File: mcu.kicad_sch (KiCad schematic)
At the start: 23 parts, among them IC3 STM32G473RCT6, J1 USB4105-GF-A-120, Y1 ECS-240-6-37B-7KM-TR

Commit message: reorganized everything and switched to 0603 as a minimum size
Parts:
- C10, C11, C24, C25, C3, C4, C5, C6, C7, C8, C9: footprint Capacitor_SMD:C_0402_1005Metric -> Capacitor_SMD:C_0603_1608Metric
- R10, R11, R15, R22, R23, R9: footprint Resistor_SMD:R_0402_1005Metric -> Resistor_SMD:R_0603_1608Metric
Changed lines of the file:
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@@
 			)
 		)
-		(property "Footprint" "Resistor_SMD:R_0402_1005Metric"
+		(property "Footprint" "Resistor_SMD:R_0603_1608Metric"
 			(at 82.55 72.898 90)
 			(effects
@@
 			)
 		)
-		(property "Datasheet" "https://www.lcsc.com/datasheet/C60490.pdf"
+		(property "Datasheet" "~"
 			(at 82.55 71.12 0)
 			(effects
@@
 			)
 		)
-		(property "Footprint" "Capacitor_SMD:C_0402_1005Metric"
+		(property "Footprint" "Capacitor_SMD:C_0603_1608Metric"
 			(at 25.4 81.5848 0)
 			(effects
@@
 			)
 		)
-		(property "Datasheet" "https://www.lcsc.com/datasheet/C76984.pdf"
+		(property "Datasheet" "~"
 			(at 21.59 82.55 0)
 			(effects
@@
 		)
 		(instances
-			(project ""
+			(project "fcg4"
 				(path "/ebe93c2f-0aae-4f69-99fc-930f63b0ac94/dd494bae-08c6-4b46-92c8-f2c39e9b21e0"
 					(reference "IC3")
@@
 			)
 		)
-		(property "Footprint" "Capacitor_SMD:C_0402_1005Metric"
+		(property "Footprint" "Capacitor_SMD:C_0603_1608Metric"
 			(at 27.6352 111.76 0)
 			(effects
@@
 			)
 		)
-		(property "Datasheet" "https://www.lcsc.com/datasheet/C76984.pdf"
+		(property "Datasheet" "~"
 			(at 26.67 107.95 0)
 			(effects
@@
 			)
 		)
-		(property "Footprint" "Capacitor_SMD:C_0402_1005Metric"
+		(property "Footprint" "Capacitor_SMD:C_0603_1608Metric"
 			(at 106.9848 182.88 0)
 			(effects
@@
 			)
 		)
-		(property "Datasheet" "https://www.lcsc.com/datasheet/C1518208.pdf"
+		(property "Datasheet" "~"
 			(at 107.95 186.69 0)
 			(effects
@@
 			)
 		)
-		(property "Footprint" "Capacitor_SMD:C_0402_1005Metric"
+		(property "Footprint" "Capacitor_SMD:C_0603_1608Metric"
 			(at 243.5352 34.29 0)
 			(effects
@@
 			)
 		)
-		(property "Datasheet" "https://www.lcsc.com/datasheet/C77020.pdf"
+		(property "Datasheet" "~"
 			(at 242.57 30.48 0)
 			(effects
@@
 		)
 		(instances
-			(project ""
+			(project "fcg4"
 				(path "/ebe93c2f-0aae-4f69-99fc-930f63b0ac94/dd494bae-08c6-4b46-92c8-f2c39e9b21e0"
 					(reference "FL1")
@@
 			)
 		)
-		(property "Footprint" "Resistor_SMD:R_0402_1005Metric"
+		(property "Footprint" "Resistor_SMD:R_0603_1608Metric"
 			(at 68.58 66.548 90)
 			(effects
@@
 			)
 		)
-		(property "Datasheet" "https://www.lcsc.com/datasheet/C60490.pdf"
+		(property "Datasheet" "~"
 			(at 68.58 64.77 0)
 			(effects
@@
 			)
 		)
-		(property "Footprint" "Capacitor_SMD:C_0402_1005Metric"
+		(property "Footprint" "Capacitor_SMD:C_0603_1608Metric"
 			(at 262.5852 34.29 0)
 			(effects
@@
 			)
 		)
-		(property "Datasheet" "https://www.lcsc.com/datasheet/C77020.pdf"
+		(property "Datasheet" "~"
 			(at 261.62 30.48 0)
 			(effects
@@
 			)
 		)
-		(property "Footprint" "Capacitor_SMD:C_0402_1005Metric"
+		(property "Footprint" "Capacitor_SMD:C_0603_1608Metric"
 			(at 256.2352 34.29 0)
 			(effects
@@
 			)
 		)
-		(property "Datasheet" "https://www.lcsc.com/datasheet/C77020.pdf"
+		(property "Datasheet" "~"
 			(at 255.27 30.48 0)
 			(effects
@@
 		)
 		(instances
-			(project ""
+			(project "fcg4"
 				(path "/ebe93c2f-0aae-4f69-99fc-930f63b0ac94/dd494bae-08c6-4b46-92c8-f2c39e9b21e0"
 					(reference "Y1")
@@
 			)
 		)
-		(property "Footprint" "Capacitor_SMD:C_0402_1005Metric"
+		(property "Footprint" "Capacitor_SMD:C_0603_1608Metric"
 			(at 98.0948 182.88 0)
 			(effects
@@
 			)
 		)
-		(property "Datasheet" "https://www.lcsc.com/datasheet/C77020.pdf"
+		(property "Datasheet" "~"
 			(at 99.06 186.69 0)
 			(effects
@@
 		)
 		(instances
-			(project ""
+			(project "fcg4"
 				(path "/ebe93c2f-0aae-4f69-99fc-930f63b0ac94/dd494bae-08c6-4b46-92c8-f2c39e9b21e0"
 					(reference "C3")
@@
 			)
 		)
-		(property "Footprint" "Capacitor_SMD:C_0402_1005Metric"
+		(property "Footprint" "Capacitor_SMD:C_0603_1608Metric"
 			(at 249.8852 34.29 0)
 			(effects
@@
 			)
 		)
-		(property "Datasheet" "https://www.lcsc.com/datasheet/C77020.pdf"
+		(property "Datasheet" "~"
 			(at 248.92 30.48 0)
 			(effects
@@
 		)
 		(instances
-			(project ""
+			(project "fcg4"
 				(path "/ebe93c2f-0aae-4f69-99fc-930f63b0ac94/dd494bae-08c6-4b46-92c8-f2c39e9b21e0"
 					(reference "JP1")
@@
 			)
 		)
-		(property "Footprint" "Capacitor_SMD:C_0402_1005Metric"
+		(property "Footprint" "Capacitor_SMD:C_0603_1608Metric"
 			(at 114.6048 179.07 0)
 			(effects
@@
 			)
 		)
-		(property "Datasheet" "https://www.lcsc.com/datasheet/C77020.pdf"
+		(property "Datasheet" "~"
 			(at 115.57 182.88 0)
 			(effects
@@
 			)
 		)
-		(property "Footprint" "Capacitor_SMD:C_0402_1005Metric"
+		(property "Footprint" "Capacitor_SMD:C_0603_1608Metric"
 			(at 124.7648 179.07 0)
 			(effects
@@
 			)
 		)
-		(property "Datasheet" "https://www.lcsc.com/datasheet/C1518208.pdf"
+		(property "Datasheet" "~"
 			(at 125.73 182.88 0)
 			(effects
@@
 			)
 		)
-		(property "Footprint" "Resistor_SMD:R_0402_1005Metric"
+		(property "Footprint" "Resistor_SMD:R_0603_1608Metric"
 			(at 106.68 65.278 90)
 			(effects
@@
 			)
 		)
-		(property "Datasheet" "https://www.lcsc.com/datasheet/C60490.pdf"
+		(property "Datasheet" "~"
 			(at 106.68 63.5 0)
 			(effects
@@
 		)
 		(instances
-			(project ""
+			(project "fcg4"
 				(path "/ebe93c2f-0aae-4f69-99fc-930f63b0ac94/dd494bae-08c6-4b46-92c8-f2c39e9b21e0"
 					(reference "J1")
@@
 			)
 		)
-		(property "Footprint" "Resistor_SMD:R_0402_1005Metric"
+		(property "Footprint" "Resistor_SMD:R_0603_1608Metric"
 			(at 194.31 102.108 90)
 			(effects
@@
 			)
 		)
-		(property "Datasheet" "https://www.lcsc.com/datasheet/C105872.pdf"
+		(property "Datasheet" "~"
 			(at 194.31 100.33 0)
 			(effects
@@
 		)
 		(instances
-			(project ""
+			(project "fcg4"
 				(path "/ebe93c2f-0aae-4f69-99fc-930f63b0ac94/dd494bae-08c6-4b46-92c8-f2c39e9b21e0"
 					(reference "R10")
@@
 			)
 		)
-		(property "Footprint" "Capacitor_SMD:C_0402_1005Metric"
+		(property "Footprint" "Capacitor_SMD:C_0603_1608Metric"
 			(at 35.56 127.3048 0)
 			(effects
@@
 			)
 		)
-		(property "Datasheet" "https://www.lcsc.com/datasheet/C77020.pdf"
+		(property "Datasheet" "~"
 			(at 31.75 128.27 0)
 			(effects
@@
 			)
 		)
-		(property "Footprint" "Resistor_SMD:R_0402_1005Metric"
+		(property "Footprint" "Resistor_SMD:R_0603_1608Metric"
 			(at 194.31 104.648 90)
 			(effects
@@
 			)
 		)
-		(property "Datasheet" "https://www.lcsc.com/datasheet/C105872.pdf"
+		(property "Datasheet" "~"
 			(at 194.31 102.87 0)
 			(effects
@@
 			)
 		)
-		(property "Footprint" "Resistor_SMD:R_0402_1005Metric"
+		(property "Footprint" "Resistor_SMD:R_0603_1608Metric"
 			(at 36.83 104.648 90)
 			(effects
@@
 			)
 		)
-		(property "Datasheet" "https://www.lcsc.com/datasheet/C185439.pdf"
+		(property "Datasheet" "~"
 			(at 36.83 102.87 0)
 			(effects
@@
 		)
 		(instances
-			(project ""
+			(project "fcg4"
 				(path "/ebe93c2f-0aae-4f69-99fc-930f63b0ac94/dd494bae-08c6-4b46-92c8-f2c39e9b21e0"
 					(reference "R9")

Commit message: update routing
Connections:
- no-connect marks 2 -> 14
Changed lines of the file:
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@@
+	)
+	(no_connect
+		(at 113.03 130.81)
+	)
+	(no_connect
+		(at 59.69 130.81)
 	)
 	(no_connect
@@
 	)
 	(no_connect
+		(at 85.09 168.91)
+	)
+	(no_connect
+		(at 113.03 135.89)
+	)
+	(no_connect
+		(at 59.69 133.35)
+	)
+	(no_connect
+		(at 90.17 90.17)
+	)
+	(no_connect
+		(at 82.55 168.91)
+	)
+	(no_connect
+		(at 92.71 168.91)
+	)
+	(no_connect
+		(at 113.03 133.35)
+	)
+	(no_connect
+		(at 59.69 138.43)
+	)
+	(no_connect
 		(at 234.95 106.68)
 	)
+	(no_connect
+		(at 92.71 90.17)
+	)
+	(no_connect
+		(at 59.69 135.89)
+	)
 	(wire

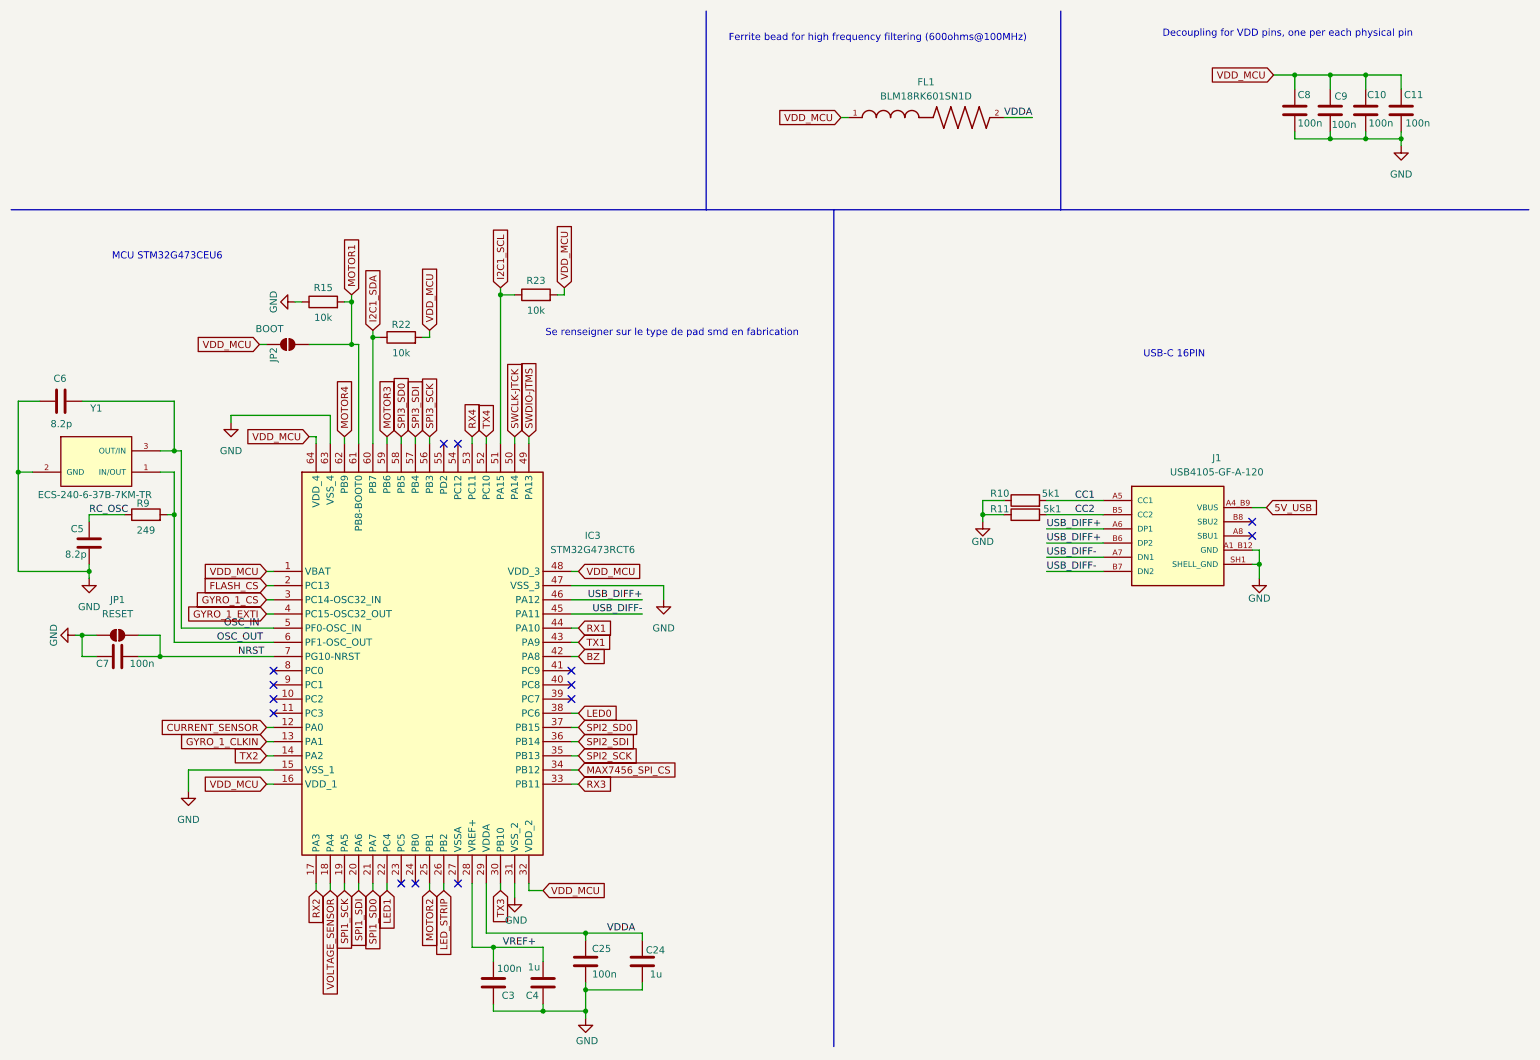
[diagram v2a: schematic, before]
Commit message: changed barometer to BMP580 and completed BOM
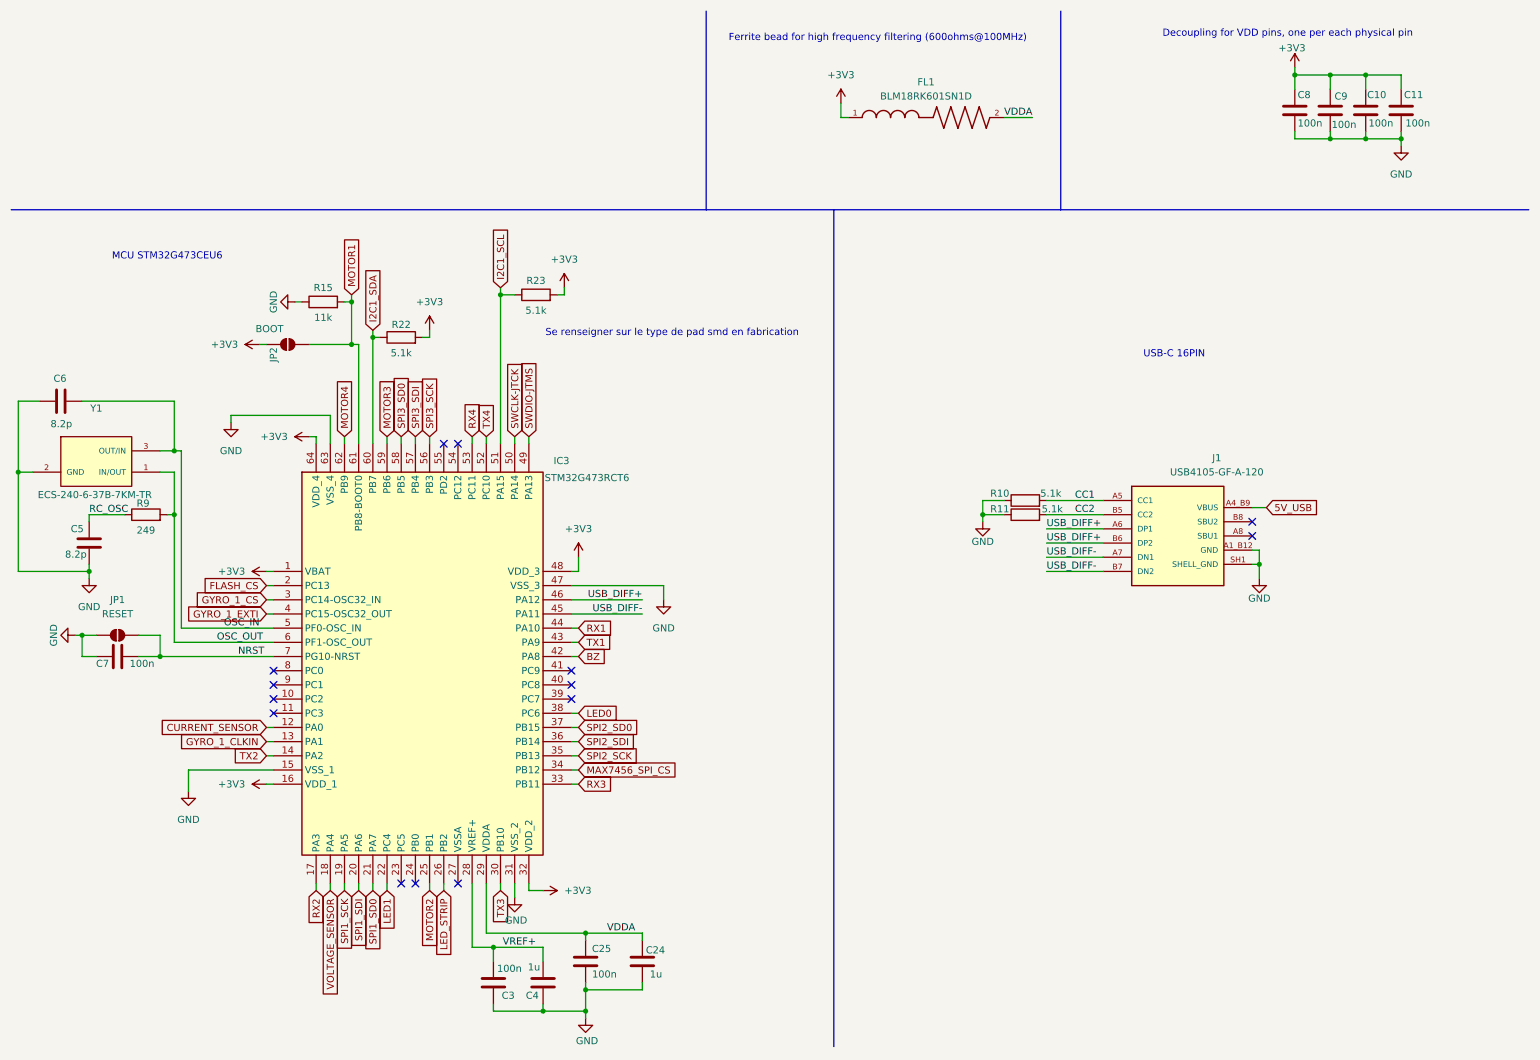
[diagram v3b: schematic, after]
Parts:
- C10, C11, C25, C3, C7, C8, C9: LCSC Part Name C77020 -> C1591; Manufacturer_Name muRata -> Samsung Electro-Mechanics; Manufacturer_Part_Number GRM155R71H104KE14D -> CL10B104KB8NNNC
- C24, C4: LCSC Part Name C1518208 -> C5199872; Manufacturer_Name muRata -> Samsung Electro-Mechanics; Manufacturer_Part_Number GRM155R61H105KE05D -> CL10B105KB8NQNC
- C5, C6: LCSC Part Name C76984 -> C277519; Manufacturer_Name muRata -> YAGEO; Manufacturer_Part_Number GRM1555C1H8R2CA01D -> CC0603CRNPO9BN8R2
- IC3: LCSC Part Name (none) -> C529361
- R10, R11: value 5k1 -> 5.1k; LCSC Part Name C105872 -> C2907044; Manufacturer_Name YAGEO -> FOJAN; Manufacturer_Part_Number RC0402FR-075K1L -> FRC0603F5101TS
- R15: value 10k -> 11k; LCSC Part Name C60490 -> C25950; Manufacturer_Name YAGEO -> UNI-ROYAL; Manufacturer_Part_Number RC0402FR-0710KL -> 0603WAF1102T5E
- R22, R23: value 10k -> 5.1k; LCSC Part Name C60490 -> C2907044; Manufacturer_Name YAGEO -> FOJAN; Manufacturer_Part_Number RC0402FR-0710KL -> FRC0603F5101TS
- R9: LCSC Part Name C185439 -> C2933176; Manufacturer_Name YAGEO -> FOJAN; Manufacturer_Part_Number RC0402FR-07249RL -> FRC0603F2490TS
- Y1: LCSC Part Name (none) -> C5213675
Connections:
- net VDD_MCU renamed +3V3

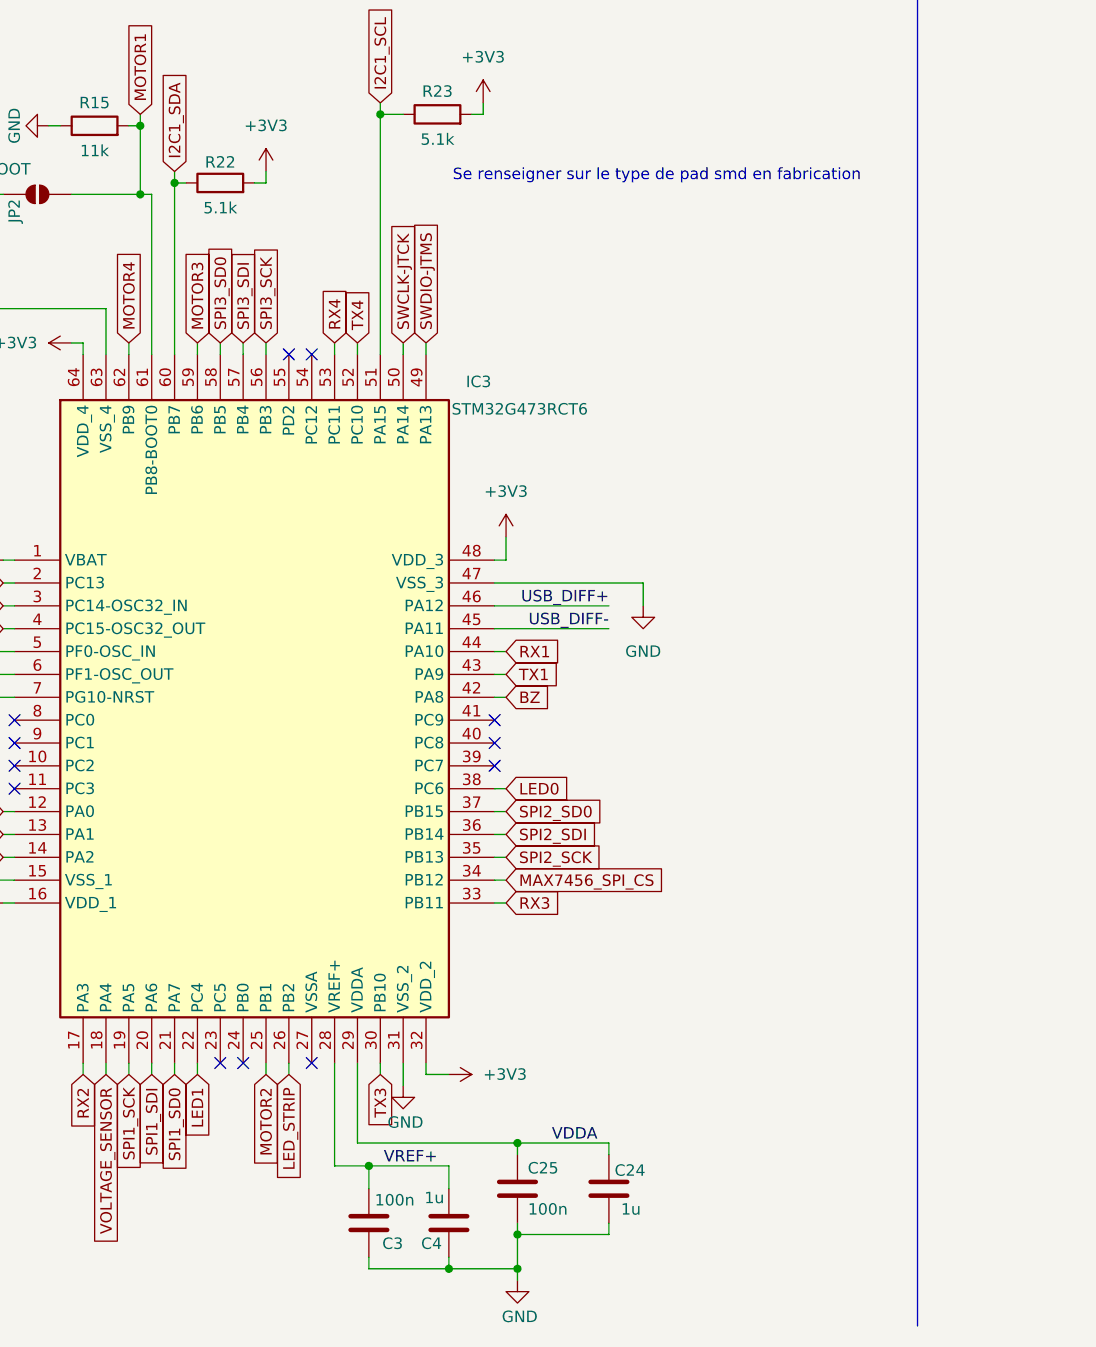
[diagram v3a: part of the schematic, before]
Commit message: switch IMU to BMI270
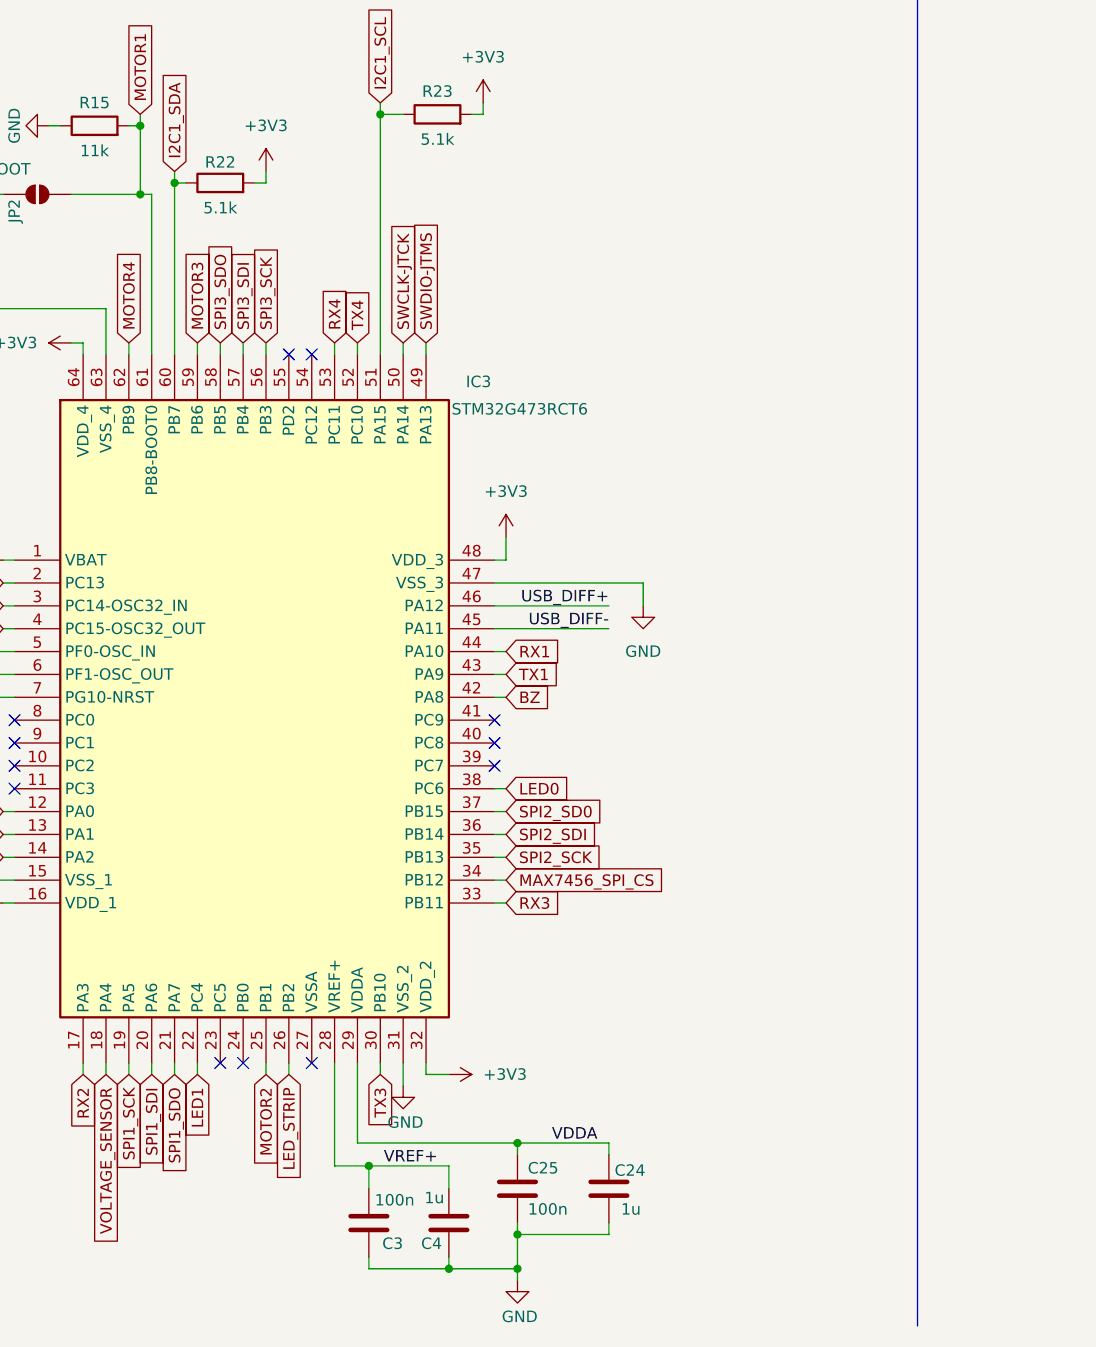
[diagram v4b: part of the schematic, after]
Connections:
- net SPI1_SD0 renamed SPI1_SDO
- net SPI3_SD0 renamed SPI3_SDO
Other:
- note removed: "Se renseigner sur le type de pad smd en fabrication"
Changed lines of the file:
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@@
 	(generator_version "9.0")
 	(paper "A4")
-	(text "Se renseigner sur le type de pad smd en fabrication"
-		(exclude_from_sim no)
-		(at 131.064 70.358 0)
-		(effects
-			(font
-				(size 1.27 1.27)
-			)
-		)
-	)
 	(text "USB-C 16PIN "
 		(exclude_from_sim no)
@@
 		)
 	)
-	(global_label "SPI3_SD0"
+	(global_label "SPI3_SDO"
 		(shape input)
 		(at 82.55 88.9 90)
@@
 		)
 		(property "Intersheetrefs" "${INTERSHEET_REFS}"
-			(at 82.55 76.9644 90)
+			(at 82.55 76.8434 90)
 			(effects
 				(font
@@
 		)
 	)
-	(global_label "SPI1_SD0"
+	(global_label "SPI1_SDO"
 		(shape input)
 		(at 77.47 170.18 270)
@@
 		)
 		(property "Intersheetrefs" "${INTERSHEET_REFS}"
-			(at 77.47 182.1156 90)
+			(at 77.47 182.2366 90)
 			(effects
 				(font
